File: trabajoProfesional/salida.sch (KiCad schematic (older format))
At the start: 14 parts

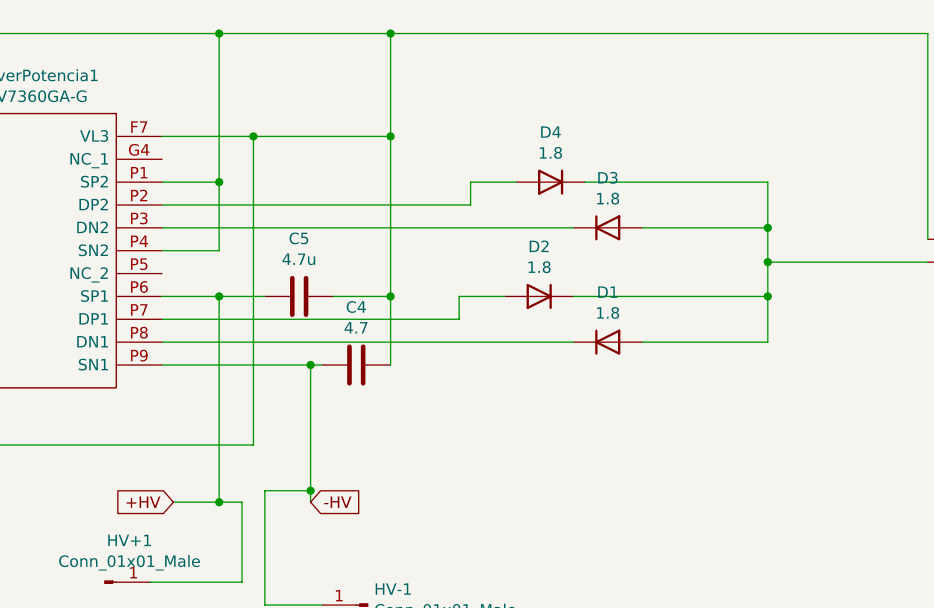
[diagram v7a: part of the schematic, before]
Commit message: se agregan los nuevos tamanios de componentes
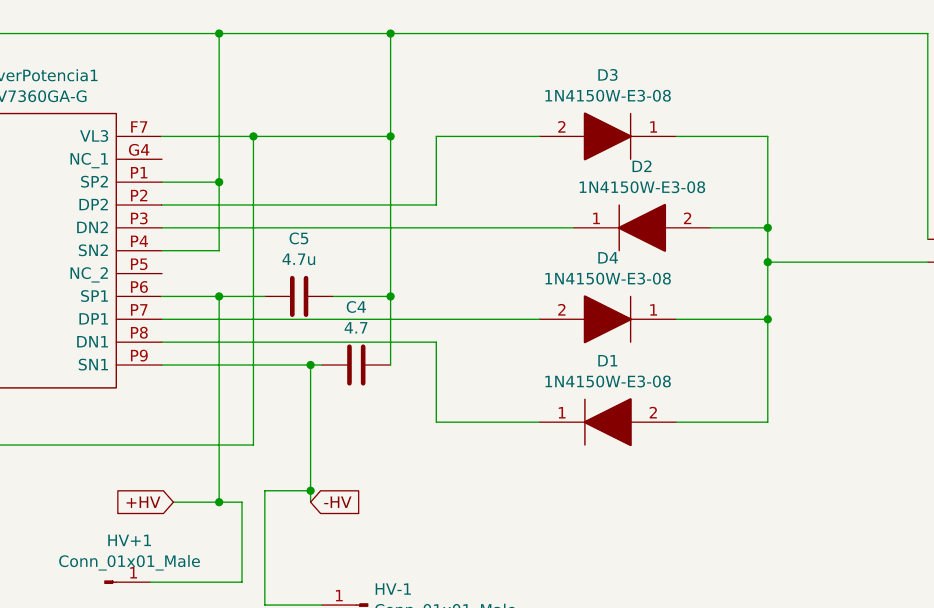
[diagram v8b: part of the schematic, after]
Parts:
- removed D1, D2, D3, D4: 1.8, Diode_SMD:D_SOD-123, symbol Device:D
- added D1, D2, D3, D4: 1N4150W-E3-08, Diodo1N4150W-e3-08:SOD3716X135N, symbol Diodo1N4150W-e3-08:1N4150W-E3-08
- C1, C2, C3, C4, C5: footprint Capacitor_SMD:C_0201_0603Metric -> Capacitor_SMD:C_0805_2012Metric
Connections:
- net at PiezoElectrico1.2 (+): now also D1.2, D2.2, D3.1, D4.1
- net at DriverPotencia1.P8 (DN1): now also D1.1
- net at DriverPotencia1.P7 (DP1): now also D4.2
- net at DriverPotencia1.P2 (DP2): now also D3.2
- net at DriverPotencia1.P3 (DN2): now also D2.1
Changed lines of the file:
@@
 EESchema Schematic File Version 4
-LIBS:trabajoProfesional-cache
-EELAYER 26 0
+EELAYER 30 0
 EELAYER END
 $Descr A4 11693 8268
@@
 Wire Wire Line
 	8950 1200 6600 1200
-Wire Wire Line
-	8250 2200 8250 2050
 Connection ~ 8250 2200
 Wire Wire Line
@@
 Wire Wire Line
 	5600 1850 5850 1850
-Connection ~ 8250 2050
-Connection ~ 8250 2350
-Wire Wire Line
-	8250 2350 8250 2200
-Wire Wire Line
-	8250 2350 7400 2350
-Wire Wire Line
-	8250 2550 8250 2350
-Wire Wire Line
-	7700 2550 8250 2550
-Wire Wire Line
-	6900 2350 7100 2350
-Wire Wire Line
-	6900 2450 6900 2350
-Wire Wire Line
-	5600 2450 6900 2450
-Wire Wire Line
-	5600 2550 7400 2550
-Wire Wire Line
-	8250 2050 7700 2050
-Wire Wire Line
-	8250 1850 8250 2050
-Wire Wire Line
-	7450 1850 8250 1850
-Wire Wire Line
-	6950 1850 7150 1850
-Wire Wire Line
-	6950 1950 6950 1850
-Wire Wire Line
-	5600 1950 6950 1950
-Wire Wire Line
-	5600 2050 7400 2050
-$Comp
-L Device:D D?
-U 1 1 5F3DE12E
-P 7550 2550
-AR Path="/5F3DE12E" Ref="D?"  Part="1"
-AR Path="/5F3D0683/5F3DE12E" Ref="D1"  Part="1"
-F 0 "D1" H 7550 2767 50  0000 C CNN
-F 1 "1.8" H 7550 2676 50  0000 C CNN
-F 2 "Diode_SMD:D_SOD-123" H 7550 2550 50  0001 C CNN
-F 3 "~" H 7550 2550 50  0001 C CNN
-	1    7550 2550
-	1    0    0    -1
-$EndComp
-$Comp
-L Device:D D?
-U 1 1 5F3DE134
-P 7250 2350
-AR Path="/5F3DE134" Ref="D?"  Part="1"
-AR Path="/5F3D0683/5F3DE134" Ref="D2"  Part="1"
-F 0 "D2" H 7250 2133 50  0000 C CNN
-F 1 "1.8" H 7250 2224 50  0000 C CNN
-F 2 "Diode_SMD:D_SOD-123" H 7250 2350 50  0001 C CNN
-F 3 "~" H 7250 2350 50  0001 C CNN
-	1    7250 2350
-	-1   0    0    1
-$EndComp
-$Comp
-L Device:D D?
-U 1 1 5F3DE13A
-P 7300 1850
-AR Path="/5F3DE13A" Ref="D?"  Part="1"
-AR Path="/5F3D0683/5F3DE13A" Ref="D4"  Part="1"
-F 0 "D4" H 7300 1633 50  0000 C CNN
-F 1 "1.8" H 7300 1724 50  0000 C CNN
-F 2 "Diode_SMD:D_SOD-123" H 7300 1850 50  0001 C CNN
-F 3 "~" H 7300 1850 50  0001 C CNN
-	1    7300 1850
-	-1   0    0    1
-$EndComp
-$Comp
-L Device:D D?
-U 1 1 5F3DE140
-P 7550 2050
-AR Path="/5F3DE140" Ref="D?"  Part="1"
-AR Path="/5F3D0683/5F3DE140" Ref="D3"  Part="1"
-F 0 "D3" H 7550 2267 50  0000 C CNN
-F 1 "1.8" H 7550 2176 50  0000 C CNN
-F 2 "Diode_SMD:D_SOD-123" H 7550 2050 50  0001 C CNN
-F 3 "~" H 7550 2050 50  0001 C CNN
-	1    7550 2050
-	1    0    0    -1
-$EndComp
+Wire Wire Line
+	5600 2550 6800 2550
+Wire Wire Line
+	5600 1950 6800 1950
 Wire Wire Line
 	6250 2650 6300 2650
@@
 F 0 "C3" V 4298 3000 50  0000 C CNN
 F 1 "4.7u" V 4389 3000 50  0000 C CNN
-F 2 "Capacitor_SMD:C_0201_0603Metric" H 4588 2850 50  0001 C CNN
+F 2 "Capacitor_SMD:C_0805_2012Metric" H 4588 2850 50  0001 C CNN
 F 3 "~" H 4550 3000 50  0001 C CNN
 	1    4550 3000
@@
 F 0 "C4" V 6198 2650 50  0000 C CNN
 F 1 "4.7" V 6289 2650 50  0000 C CNN
-F 2 "Capacitor_SMD:C_0201_0603Metric" H 6488 2500 50  0001 C CNN
+F 2 "Capacitor_SMD:C_0805_2012Metric" H 6488 2500 50  0001 C CNN
 F 3 "~" H 6450 2650 50  0001 C CNN
 	1    6450 2650
@@
 F 0 "C5" V 5948 2350 50  0000 C CNN
 F 1 "4.7u" V 6039 2350 50  0000 C CNN
-F 2 "Capacitor_SMD:C_0201_0603Metric" H 6238 2200 50  0001 C CNN
+F 2 "Capacitor_SMD:C_0805_2012Metric" H 6238 2200 50  0001 C CNN
 F 3 "~" H 6200 2350 50  0001 C CNN
 	1    6200 2350
@@
 F 0 "C2" V 3198 2350 50  0000 C CNN
 F 1 "4.7u" V 3289 2350 50  0000 C CNN
-F 2 "Capacitor_SMD:C_0201_0603Metric" H 3488 2200 50  0001 C CNN
+F 2 "Capacitor_SMD:C_0805_2012Metric" H 3488 2200 50  0001 C CNN
 F 3 "~" H 3450 2350 50  0001 C CNN
 	1    3450 2350
@@
 F 0 "C1" V 3398 2050 50  0000 C CNN
 F 1 "4.7u" V 3489 2050 50  0000 C CNN
-F 2 "Capacitor_SMD:C_0201_0603Metric" H 3688 1900 50  0001 C CNN
+F 2 "Capacitor_SMD:C_0805_2012Metric" H 3688 1900 50  0001 C CNN
 F 3 "~" H 3650 2050 50  0001 C CNN
 	1    3650 2050
@@
 Wire Wire Line
 	6300 3700 6050 3700
+$Comp
+L Diodo1N4150W-e3-08:1N4150W-E3-08 D1
+U 1 1 5FB3FE5F
+P 7250 2900
+F 0 "D1" H 7550 3167 50  0000 C CNN
+F 1 "1N4150W-E3-08" H 7550 3076 50  0000 C CNN
+F 2 "Diodo1N4150W-e3-08:SOD3716X135N" H 7700 2900 50  0001 L CNN
+F 3 "" H 7700 2800 50  0001 L CNN
+F 4 "Vishay 1N4150W-E3-08, SMT Small Signal Diode, 50V 200mA, 4ns, 2-Pin SOD-123" H 7700 2700 50  0001 L CNN "Description"
+F 5 "1.35" H 7700 2600 50  0001 L CNN "Height"
+F 6 "78-1N4150W-E3-08" H 7700 2500 50  0001 L CNN "Mouser Part Number"
+F 7 "https://www.mouser.co.uk/ProductDetail/Vishay-Semiconductors/1N4150W-E3-08?qs=vP9d3Jd3b8abHYnKidD6uA%3D%3D" H 7700 2400 50  0001 L CNN "Mouser Price/Stock"
+F 8 "Vishay" H 7700 2300 50  0001 L CNN "Manufacturer_Name"
+F 9 "1N4150W-E3-08" H 7700 2200 50  0001 L CNN "Manufacturer_Part_Number"
+	1    7250 2900
+	1    0    0    -1
+$EndComp
+$Comp
+L Diodo1N4150W-e3-08:1N4150W-E3-08 D3
+U 1 1 5FB409B6
+P 7850 1650
+F 0 "D3" H 8150 1383 50  0000 C CNN
+F 1 "1N4150W-E3-08" H 8150 1474 50  0000 C CNN
+F 2 "Diodo1N4150W-e3-08:SOD3716X135N" H 8300 1650 50  0001 L CNN
+F 3 "" H 8300 1550 50  0001 L CNN
+F 4 "Vishay 1N4150W-E3-08, SMT Small Signal Diode, 50V 200mA, 4ns, 2-Pin SOD-123" H 8300 1450 50  0001 L CNN "Description"
+F 5 "1.35" H 8300 1350 50  0001 L CNN "Height"
+F 6 "78-1N4150W-E3-08" H 8300 1250 50  0001 L CNN "Mouser Part Number"
+F 7 "https://www.mouser.co.uk/ProductDetail/Vishay-Semiconductors/1N4150W-E3-08?qs=vP9d3Jd3b8abHYnKidD6uA%3D%3D" H 8300 1150 50  0001 L CNN "Mouser Price/Stock"
+F 8 "Vishay" H 8300 1050 50  0001 L CNN "Manufacturer_Name"
+F 9 "1N4150W-E3-08" H 8300 950 50  0001 L CNN "Manufacturer_Part_Number"
+	1    7850 1650
+	-1   0    0    1
+$EndComp
+$Comp
+L Diodo1N4150W-e3-08:1N4150W-E3-08 D2
+U 1 1 5FB40FC0
+P 7400 2050
+F 0 "D2" H 7700 2317 50  0000 C CNN
+F 1 "1N4150W-E3-08" H 7700 2226 50  0000 C CNN
+F 2 "Diodo1N4150W-e3-08:SOD3716X135N" H 7850 2050 50  0001 L CNN
+F 3 "" H 7850 1950 50  0001 L CNN
+F 4 "Vishay 1N4150W-E3-08, SMT Small Signal Diode, 50V 200mA, 4ns, 2-Pin SOD-123" H 7850 1850 50  0001 L CNN "Description"
+F 5 "1.35" H 7850 1750 50  0001 L CNN "Height"
+F 6 "78-1N4150W-E3-08" H 7850 1650 50  0001 L CNN "Mouser Part Number"
+F 7 "https://www.mouser.co.uk/ProductDetail/Vishay-Semiconductors/1N4150W-E3-08?qs=vP9d3Jd3b8abHYnKidD6uA%3D%3D" H 7850 1550 50  0001 L CNN "Mouser Price/Stock"
+F 8 "Vishay" H 7850 1450 50  0001 L CNN "Manufacturer_Name"
+F 9 "1N4150W-E3-08" H 7850 1350 50  0001 L CNN "Manufacturer_Part_Number"
+	1    7400 2050
+	1    0    0    -1
+$EndComp
+$Comp
+L Diodo1N4150W-e3-08:1N4150W-E3-08 D4
+U 1 1 5FB41538
+P 7850 2450
+F 0 "D4" H 8150 2183 50  0000 C CNN
+F 1 "1N4150W-E3-08" H 8150 2274 50  0000 C CNN
+F 2 "Diodo1N4150W-e3-08:SOD3716X135N" H 8300 2450 50  0001 L CNN
+F 3 "" H 8300 2350 50  0001 L CNN
+F 4 "Vishay 1N4150W-E3-08, SMT Small Signal Diode, 50V 200mA, 4ns, 2-Pin SOD-123" H 8300 2250 50  0001 L CNN "Description"
+F 5 "1.35" H 8300 2150 50  0001 L CNN "Height"
+F 6 "78-1N4150W-E3-08" H 8300 2050 50  0001 L CNN "Mouser Part Number"
+F 7 "https://www.mouser.co.uk/ProductDetail/Vishay-Semiconductors/1N4150W-E3-08?qs=vP9d3Jd3b8abHYnKidD6uA%3D%3D" H 8300 1950 50  0001 L CNN "Mouser Price/Stock"
+F 8 "Vishay" H 8300 1850 50  0001 L CNN "Manufacturer_Name"
+F 9 "1N4150W-E3-08" H 8300 1750 50  0001 L CNN "Manufacturer_Part_Number"
+	1    7850 2450
+	-1   0    0    1
+$EndComp
+Wire Wire Line
+	7850 2900 8250 2900
+Wire Wire Line
+	7250 2900 6800 2900
+Wire Wire Line
+	6800 2900 6800 2550
+Wire Wire Line
+	8250 2200 8250 2450
+Wire Wire Line
+	7850 2450 8250 2450
+Connection ~ 8250 2450
+Wire Wire Line
+	8250 2450 8250 2900
+Wire Wire Line
+	5600 2450 7250 2450
+Wire Wire Line
+	7850 1650 8250 1650
+Wire Wire Line
+	7250 1650 6800 1650
+Wire Wire Line
+	6800 1650 6800 1950
+Wire Wire Line
+	5600 2050 7400 2050
+Wire Wire Line
+	8000 2050 8250 2050
+Wire Wire Line
+	8250 1650 8250 2050
+Connection ~ 8250 2050
+Wire Wire Line
+	8250 2050 8250 2200
 $EndSCHEMATC
